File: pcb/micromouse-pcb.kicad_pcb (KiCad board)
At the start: 4 copper layers, 100 x 120 mm, 179 parts, among them J1 BATT_IN_2S, J5 MOTOR_A_N20_ENCODER, J6 MOTOR_B_N20_ENCODER, J7 USB-C rear (GCT USB4105; VBUS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, J8 JTAG_1x6 (3V3,TMS,TCK,TDO,TDI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, J9 BALANCE_2S, Q1 Q_PMOS reverse guard (DMP3098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, Q16 BSS138 (real part; Q_NMOS_GSD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, Q17 BSS138 (real part; Q_NMOS_GSD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, Q18 BSS138 (real part; Q_NMOS_GSD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, Q19 BSS138 (real part; Q_NMOS_GSD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, Q2 PT334-6B (5mm filtered PT; LO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, Q20 BSS138 (real part; Q_NMOS_GSD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, Q21 BSS138 (real part; Q_NMOS_GSD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, Q22 BSS138 (real part; Q_NMOS_GSD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, Q23 BSS138 (real part; Q_NMOS_GSD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, Q24 BSS138 (real part; Q_NMOS_GSD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, Q25 BSS138 (real part; Q_NMOS_GSD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, Q26 BSS138 (real part; Q_NMOS_GSD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, Q27 BSS138 (real part; Q_NMOS_GSD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, Q28 BSS84 (PMOS indicator driver;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, Q29 BSS84 (PMOS indicator driver;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, Q3 PT334-6B (5mm filtered PT; LO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, Q30 BSS84 (PMOS indicator driver;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, Q31 BSS84 (PMOS indicator driver;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, Q32 BSS84 (PMOS indicator driver;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, Q33 BSS84 (PMOS indicator driver;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, Q4 PT334-6B (5mm filtered PT; LO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, Q5 PT334-6B (5mm filtered PT; LO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, Q6 PT334-6B (5mm filtered PT; LO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, Q7 PT334-6B (5mm filtered PT; LO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, SW1 BTN_A (start / BOOT), SW2 RESET, SW3 BTN_B, SW4 BTN_C, SW5 PWR ALL (PCM12SMTR slide; sli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, SW6 PWR MOTORS (PCM12SMTR slide; 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, U1 AP63203WU-7 (fixed 3.3V 2A bu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, U2 TB6612FNG, U3 ESP32-S3-WROOM-1-N8R2 (quad P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, U4 CD74HC4067M, U6 USBLC6-2SC6 (SOT-23-6; 2P6 ba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, U7 TPS54302DDCR (6.0V/3A motor b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, U8 BNO055 (9-axis IMU + fusion; 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

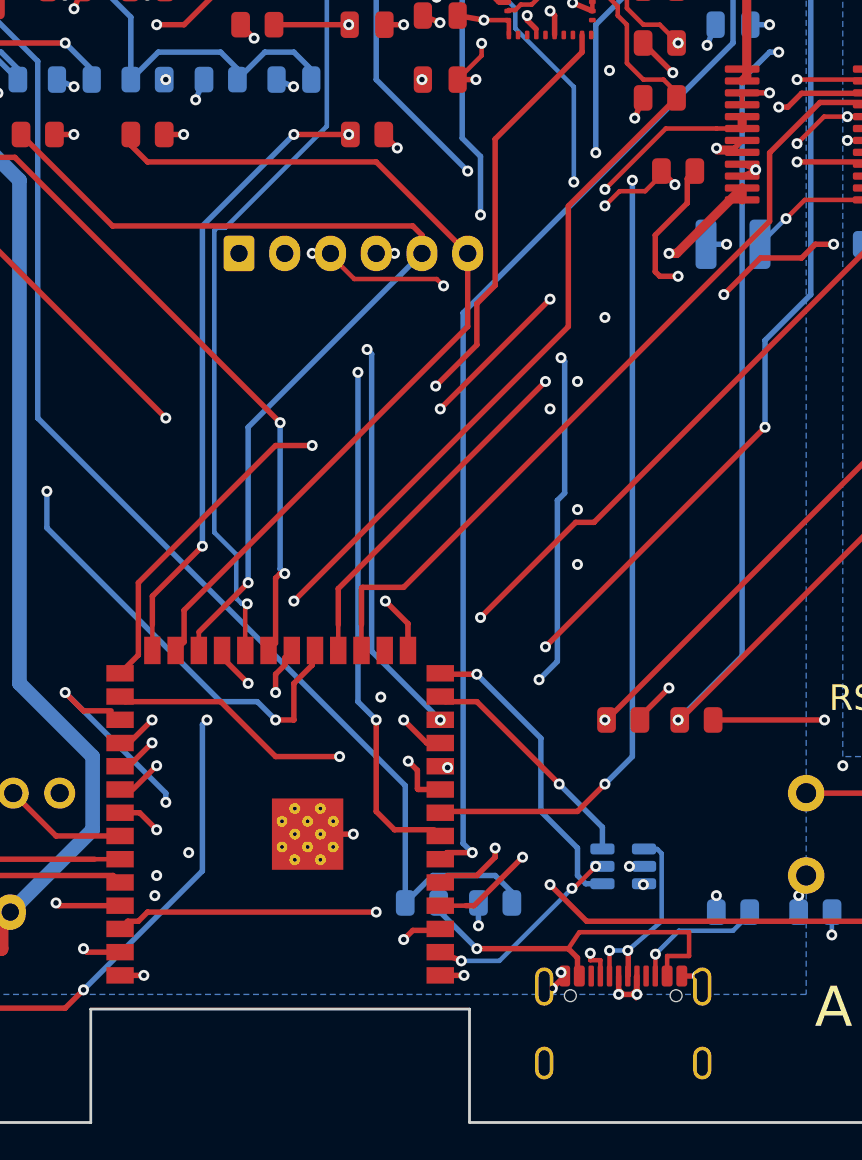
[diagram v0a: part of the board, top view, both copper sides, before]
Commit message: Rev 7 (2/n): antenna audit + USB-C overhang + J5 forward move
ESP32/antenna guideline audit (user-requested, done FIRST since it constrains
rear-region placement): antenna-over-cutout is Espressif's preferred option and
the meander keepout ribbon (x31-39) is correct; copper near the module is under
the shielded body region (allowed) or the module's own GND-pad stitching
(required). Two documented deviations: J7 USB shell 4.08mm lateral of the
notch east edge, SW6 body 5.0mm west -- inherent to rear-USB + rear-antenna
requirements; acceptable for robot telemetry (fix would be a full USB-pocket
rebuild for ~4mm gain). C10/C8 decoupling landing zone chosen at x~46.5
(east of module edge, outside ribbon).

J7 USB-C +1.5mm rearward (user req: cable overmold must clear the PCB edge):
footprint shifted 115.675->117.175; the behind-row USB_DP_C network translated
with it; CC2 re-routed fresh (F stub + via (55.75,114.8) + B dogleg around the
GND via at (58.05,112)); 7 pad-row stitch stubs; zero-length VBUS orphans
dropped. Mouth now overhangs the rear edge ~1.5mm.

J5 left motor connector forward (33,72.5)->(33,70) (user req: clears the motor
body, gap 1.6->4.1mm): 22 items stripped (3 foreign -45deg diagonals passed
EXACTLY through new pin holes; XH pad annulus r~0.95 caught 3 more in round 2),
9 A* reroutes (MOTA_P/N, ENC1_A/B, ENC2_A, LINE_EMIT, ESP_EN, WALL_EMIT_SIDE,
BIN2, PLUS3V3 pin3->R7.2), ENC1_A re-pathed to the pad itself, old-pad orphans
+ 2 exposed danglers cleaned (all ratsnest-gated).

State: 12 known courtyard errors (front cluster, next step), 0 warnings,
0 unconnected, 0 parity, ratsnest 0.

Co-Authored-By: Claude Opus 4.8 (1M context) <noreply@anthropic.com>
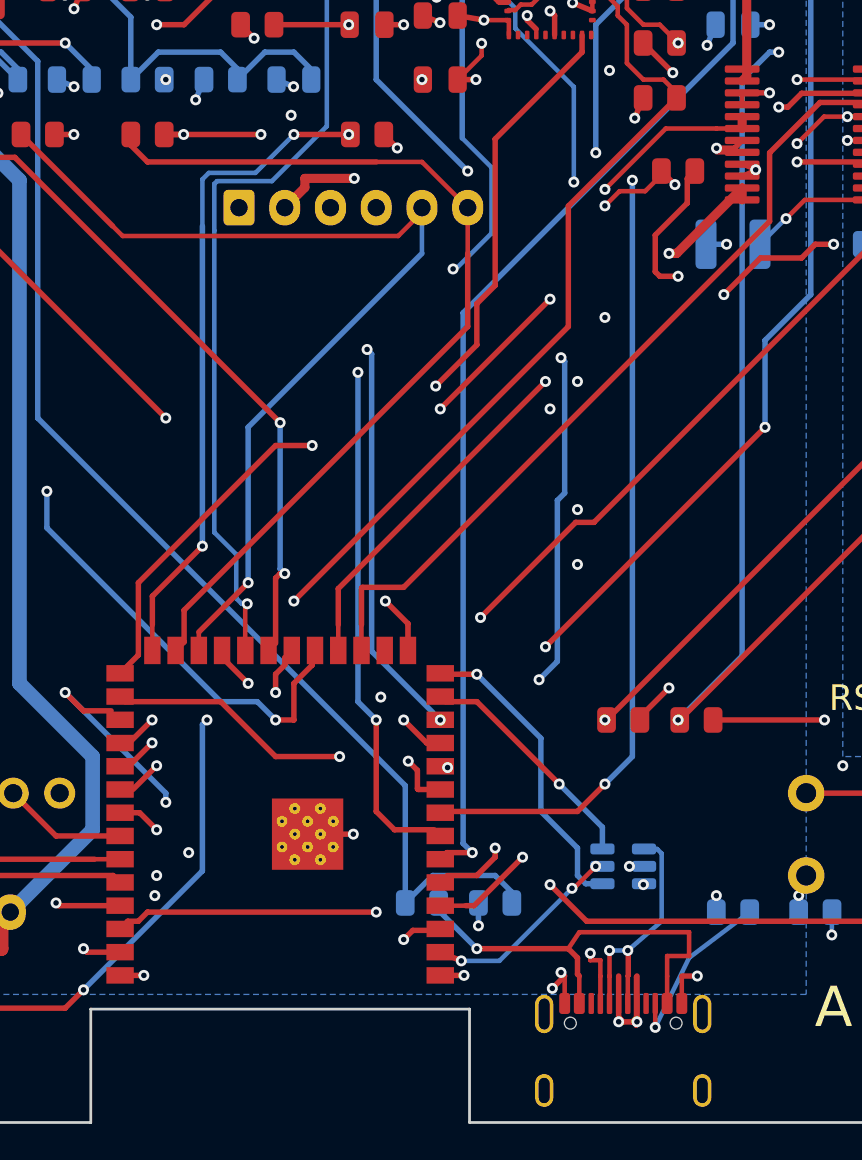
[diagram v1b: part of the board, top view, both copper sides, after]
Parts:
- moved J5 2.50 mm to (33.0, 70.0)
- moved J7 1.50 mm to (54.0, 117.2)
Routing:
- net PLUS3V3: track 175.3 -> 161.7 mm, vias 73 -> 72
- net USB_DP_C: track 14.2 -> 23.2 mm
- net WALL_EMIT_SIDE: track 69.2 -> 73.7 mm
- net USB_VBUS: track 20.8 -> 23.8 mm
- net USB_DM_C: track 12.2 -> 15.2 mm
- net ENC1_A: track 51.9 -> 54.2 mm
- net Net-(J7-CC2): track 7.37 -> 9.67 mm
- net GND: track 95.3 -> 97.3 mm, vias 73 -> 72
- net Net-(J7-CC1): track 16.8 -> 18.3 mm
- net BIN2: track 63.6 -> 65.1 mm
- net LINE_EMIT: track 66.6 -> 68.1 mm
- net ENC1_B: track 49.8 -> 51.2 mm
- net ESP_EN: track 106.2 -> 107.2 mm
- net MOTA_N: track 29.8 -> 29.1 mm, vias 1 -> 2
- net MOTA_P: track 44.3 -> 44.5 mm, vias 2 -> 3

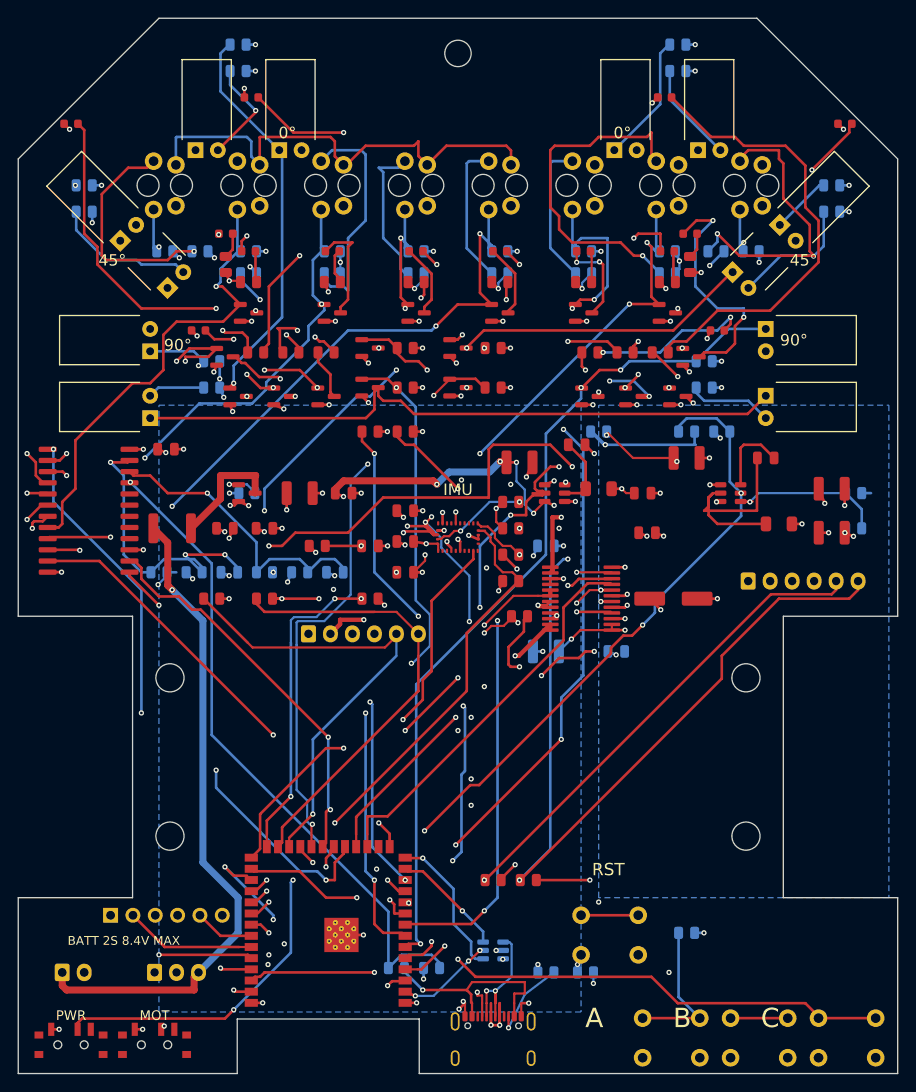
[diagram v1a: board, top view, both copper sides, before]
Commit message: Rev 7 (3/n): PATH A DONE -- verify_drc PASS: 0 errors / 0 warnings
The core front-cluster redesign, all in-place with the routing preserved:

- Front wall sensors D1/Q2/D2/Q3 rotated 90deg into the line-array gaps
  (vertical pad pairs at the gap centers; 0-deg aim and bent-optic silk
  outlines unchanged -- hole-pair centers identical). 64 items stripped,
  16 A* reroutes (sensor nets pad-chained + foreign relinks EMIT_LINE_K,
  LS2/LS7-Pad1), C12.2 GND pour-neck casualty re-routed to U2.10.
- Diagonal receivers Q4/Q5 rotated to 135/45 (pads perpendicular to the aim,
  same bent-lead style as the fronts; pad-pair centers still exactly on the
  det points -> 45.000deg aims preserved). WALL3/4_SENSE relinked + closures.
- D3/D4 courtyards: the tightener only handled fp_rect; their original wide
  fp_poly courtyards replaced with body-true circles (r 2.63 at the hole
  centers) -- clears both courtyards_overlap.
- Wall indicator LEDs D23-D28 moved BEHIND their sensors (user req
  MMSE-WALL-5): fronts to the line-gap columns (21.43/78.57, 19.6), diagonals
  to (8.5/91.5, 32) (also clears D25's chamfer nick, MMSE-REM-7), sides to
  (20.5/79.5, 46.5). A-nets stripped + A*-rerouted to the central drivers;
  K-pads stitched to the In1 plane with spiral-scanned vias; old stubs/vias
  cleaned text-level.
- '0deg' angle labels moved to the outline-band gaps (26.2/73.8, 12).
- Post-pass per HANDOFF 7.1: T-carrier dangler TRIMMED to its junction (not
  deleted), A* joint ends snapped onto the via at (70.5,40.5).

pcb/tools/verify_drc.py (error-inclusive severity + schematic parity +
pcbnew ratsnest):
  PASS -- 0 errors / 0 warnings / 0 unconnected / 0 parity / ratsnest 0

Remaining rev-7 scope: C10/C8 decoupling move to U3 (MMSE-SI-3), GND pours on
all possible layers (MMSE-SI-4), then full battery + fab + docs.

Co-Authored-By: Claude Opus 4.8 (1M context) <noreply@anthropic.com>
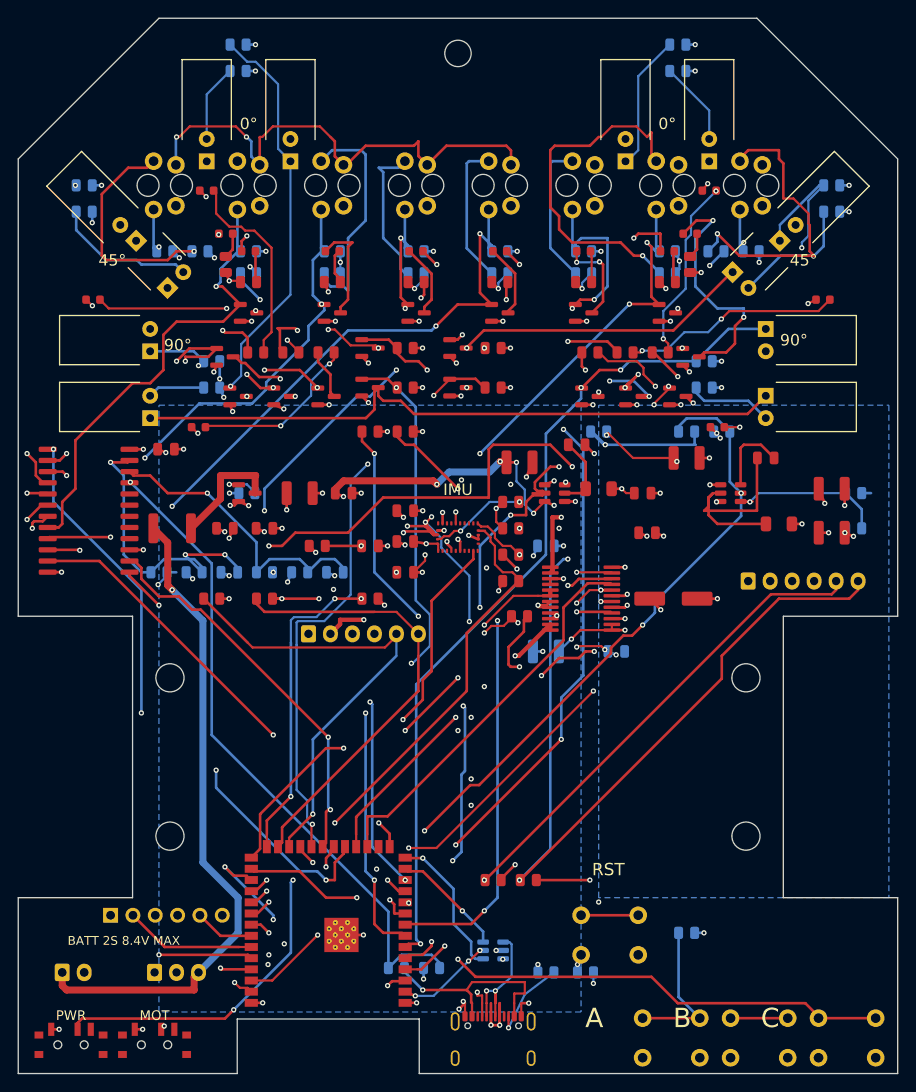
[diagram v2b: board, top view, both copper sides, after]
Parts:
- moved D25 20.2 mm to (8.50, 32.0)
- moved D26 20.2 mm to (91.5, 32.0)
- moved D23 11.8 mm to (21.4, 19.6)
- moved D24 11.8 mm to (78.6, 19.6)
- moved D27 11.0 mm to (20.5, 46.5)
- moved D28 11.0 mm to (79.5, 46.5)
- moved Q4 1.80 mm to (13.4, 25.3), turned to 135 degrees
- moved Q5 1.80 mm to (86.6, 25.3), turned to 45 degrees
- moved D1 1.80 mm to (21.4, 16.3), turned to 90 degrees
- moved Q2 1.80 mm to (30.9, 16.3), turned to 90 degrees
- moved D2 1.80 mm to (78.6, 16.3), turned to 90 degrees
- moved Q3 1.80 mm to (69.0, 16.3), turned to 90 degrees
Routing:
- net WALL4_SENSE: track 112.7 -> 157.1 mm, vias 3 -> 4
- net Net-(D24-A): track 51.8 -> 21.1 mm, vias 0 -> 2
- net WALL2_SENSE: track 158.9 -> 135.4 mm, vias 3 -> 5
- net Net-(D26-A): track 48.0 -> 24.9 mm
- net Net-(D23-A): track 44.0 -> 22.9 mm, vias 2 -> 0
- net Net-(D25-A): track 44.3 -> 25.2 mm
- net GND: track 97.3 -> 107.7 mm, vias 72 -> 74
- net EMIT_LINE_K: track 124.4 -> 128.4 mm, vias 1 -> 3
- net EMIT_FRONT_K: track 84.0 -> 80.5 mm, vias 1 -> 2
- net Net-(D27-A): track 16.1 -> 19.6 mm
- net Net-(D28-A): track 18.5 -> 21.9 mm
- net Net-(D1-A): track 12.0 -> 8.83 mm, vias 1 -> 0
- net WALL3_SENSE: track 94.6 -> 96.4 mm
- net Net-(D2-A): track 11.4 -> 9.59 mm
- net Net-(LS7-Pad1): track 38.7 -> 39.7 mm
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
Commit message: Rev 7 (4/n): decoupling at the module + GND on all possible layers -- 0/0
MMSE-SI-3: C8 (100nF) moved to (48.4,108.7), 1.5mm from U3 pin 2's 3V3 via;
C10 (10uF bulk) at (50.8,104.8), ~5mm. Was 51mm. Routed to the pin-2 via,
chained; GND pads pour-fed. (Espressif local-decoupling guideline satisfied.)

MMSE-SI-4: GND poured on F.Cu (full board) and B.Cu (remainder around the VM
pours, priority 0 vs 1) with SOLID pad connection (thermal spokes starved in
the dense clusters); GND now on F.Cu + In1 + B.Cu; In2 remains the 3V3 plane.
The WROOM antenna keepout ribbon extended from F.Cu to ALL copper layers so
no pour can enter the antenna near-field.

Post-pass: A*-joint polish (0.58mm In1 dangler chain cleaned, In2 track end
snapped onto the pin-2 via), all connectivity-gated.

verify_drc: PASS -- 0 errors / 0 warnings / 0 unconnected / 0 parity /
ratsnest 0. All rev-7 board requirements are now IN: USB-C overhang, J5
forward, indicators behind, front sensors in the line gaps (path A), exact
0/45/90 aims preserved, module decoupling local, ground on every possible
layer, antenna guidelines enforced.

Co-Authored-By: Claude Opus 4.8 (1M context) <noreply@anthropic.com>
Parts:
- moved C8 56.5 mm to (48.4, 108.7), turned to 90 degrees
- moved C10 52.1 mm to (50.8, 104.8)
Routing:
- net PLUS3V3: track 161.7 -> 227.1 mm, vias 72 -> 76
- net GND: track 107.7 -> 105.4 mm, vias 74 -> 73
- added copper zone on B.Cu, net GND
- added copper zone on F.Cu, net GND
